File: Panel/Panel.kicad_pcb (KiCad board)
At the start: 2 copper layers, 100 x 100 mm, 81 parts, among them J1 Conn_01x03, J10 Conn_01x02, J11 Conn_01x03, J12 Conn_01x03, J2 USB_C_Receptacle_USB2.0, J3 Conn_01x02, J4 Conn_02x06_Odd_Even, J5 Conn_01x07, J6 Conn_01x02, J7 Conn_01x02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

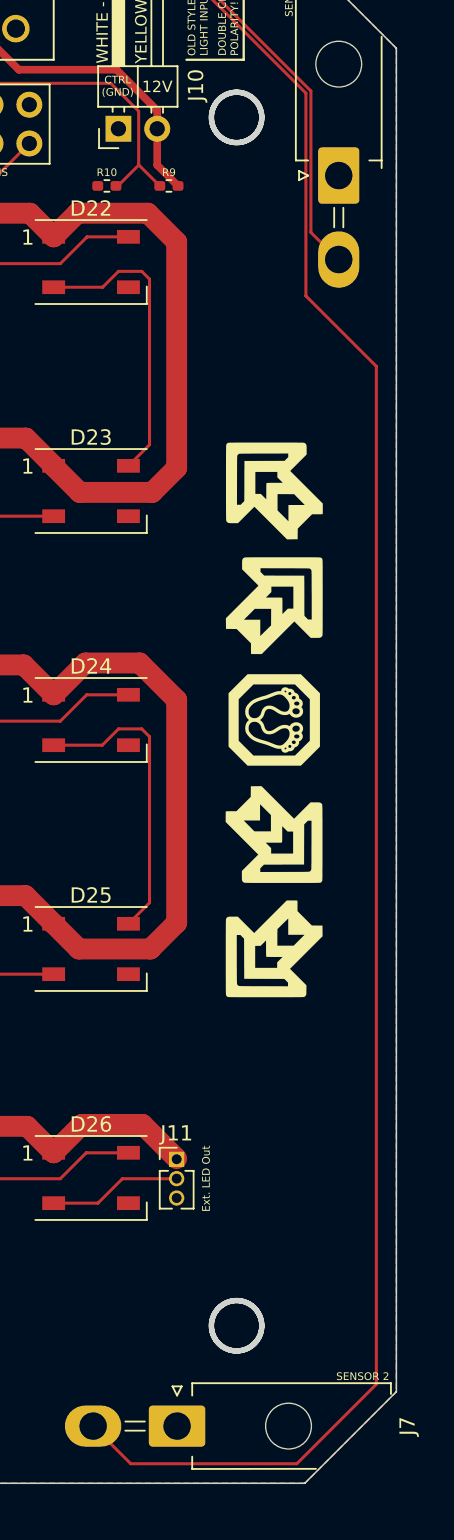
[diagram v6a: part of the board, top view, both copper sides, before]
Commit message: Fix major schematic issue and parity warnings
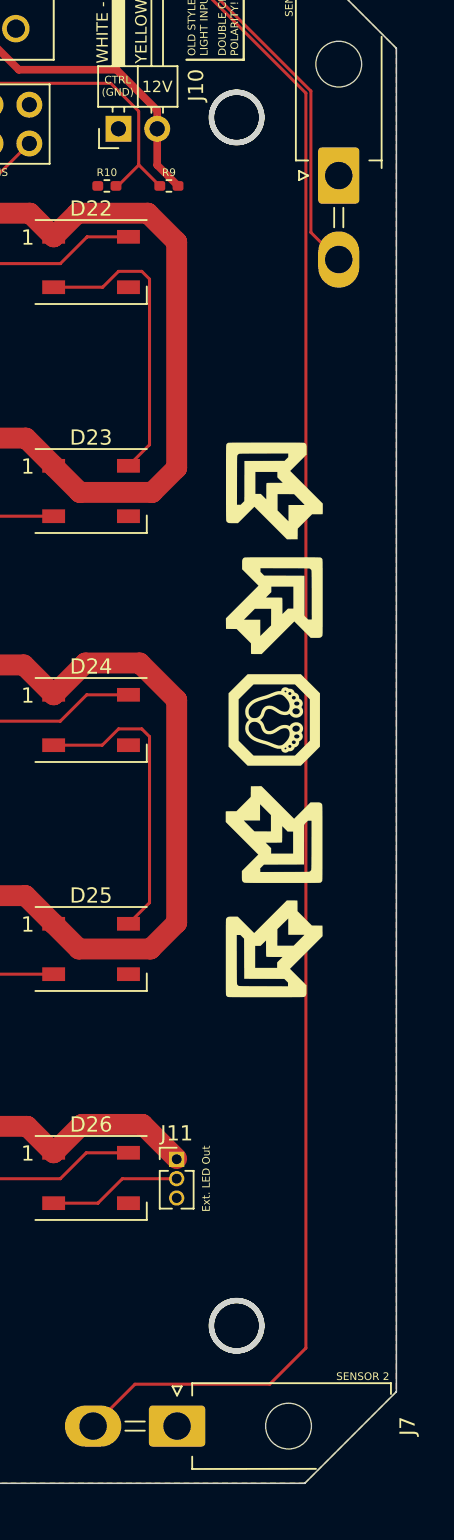
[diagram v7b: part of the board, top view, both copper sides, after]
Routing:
- net SENSOR 2: track 138.4 -> 128.5 mm
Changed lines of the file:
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@@
   (segment (start 128.07 65.478) (end 135.898448 65.478) (width 0.2) (layer "B.Cu") (net 60))
   (segment (start 126.8 66.748) (end 128.07 65.478) (width 0.2) (layer "B.Cu") (net 60))
-  (segment (start 174.073 72.219) (end 178.689 76.835) (width 0.2) (layer "F.Cu") (net 61))
-  (segment (start 178.689 143.51) (end 173.482 148.717) (width 0.2) (layer "F.Cu") (net 61))
-  (segment (start 174.073 58.935448) (end 174.073 72.219) (width 0.2) (layer "F.Cu") (net 61))
-  (segment (start 162.5988 148.717) (end 160.135 146.2532) (width 0.2) (layer "F.Cu") (net 61))
+  (segment (start 149.962 52.324) (end 167.461552 52.324) (width 0.2) (layer "F.Cu") (net 61))
+  (segment (start 147.574 54.712) (end 149.962 52.324) (width 0.2) (layer "F.Cu") (net 61))
+  (segment (start 174.073 141.141) (end 171.704 143.51) (width 0.2) (layer "F.Cu") (net 61))
+  (segment (start 174.073 58.935448) (end 174.073 141.141) (width 0.2) (layer "F.Cu") (net 61))
+  (segment (start 171.704 143.51) (end 162.8782 143.51) (width 0.2) (layer "F.Cu") (net 61))
+  (segment (start 162.8782 143.51) (end 160.135 146.2532) (width 0.2) (layer "F.Cu") (net 61))
   (segment (start 167.461552 52.324) (end 174.073 58.935448) (width 0.2) (layer "F.Cu") (net 61))
-  (segment (start 147.574 54.712) (end 149.962 52.324) (width 0.2) (layer "F.Cu") (net 61))
-  (segment (start 178.689 76.835) (end 178.689 143.51) (width 0.2) (layer "F.Cu") (net 61))
-  (segment (start 149.962 52.324) (end 167.461552 52.324) (width 0.2) (layer "F.Cu") (net 61))
-  (segment (start 173.482 148.717) (end 162.5988 148.717) (width 0.2) (layer "F.Cu") (net 61))
   (segment (start 155.266 57.404) (end 161.671 57.404) (width 0.5) (layer "F.Cu") (net 62))
   (segment (start 152.574 54.712) (end 155.266 57.404) (width 0.5) (layer "F.Cu") (net 62))

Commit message: Final touches (hopefully for real this time)
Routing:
- net SENSOR 2: track 128.5 -> 127.6 mm
- net SENSOR 1: track 50.1 -> 49.2 mm
